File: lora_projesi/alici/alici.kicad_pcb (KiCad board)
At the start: 4 copper layers, 88 x 102 mm, 127 parts, among them J1 USB-C, J2 SMA, J3 RJ45, J4 u.FL (ANA ANTEN), J5 12 V GIRIS, J6 LAMBA, J7 MICRO-SIM, J8 u.FL (YARDIMCI ANTEN, ISTEGE 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, K1 SRD-12VDC-SL-A, Q1 AO3401A, Q2 MMBT2222A, Q3 MMBT2222A, Q4 MMBT2222A, SW1 DUGME, U1 ESP32-S3-WROOM-1-N4, U10 SIM7600SA, U11 AP2112K-3.3, U12 ESDA6V1-5SC6, U4 RFM95W-915S2, U5 TPS62933DRLR, U6 TPS62933DRLR, U7 USBLC6-2SC6, U8 TXB0104PW, U9 W5500, Y1 25 MHz

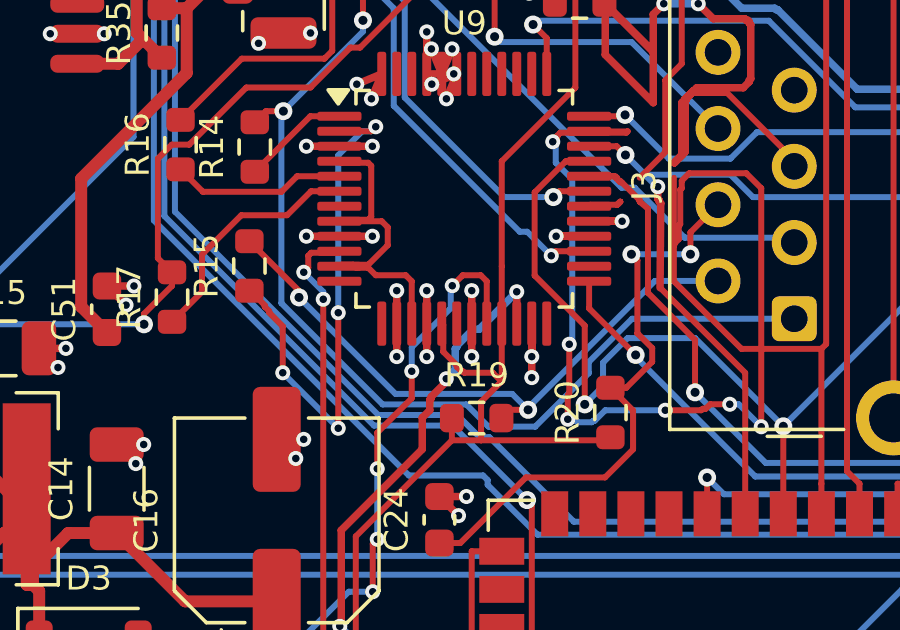
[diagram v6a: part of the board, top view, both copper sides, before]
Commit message: Alici: pin 16 dis toprak via kaldirildi, yonlendirme suruyor
Co-Authored-By: Claude Sonnet 5.5 <noreply@anthropic.com>
Claude-Session: https://claude.ai/code/session_01Q71gHQtKJ86ZE2CtYTYSwP
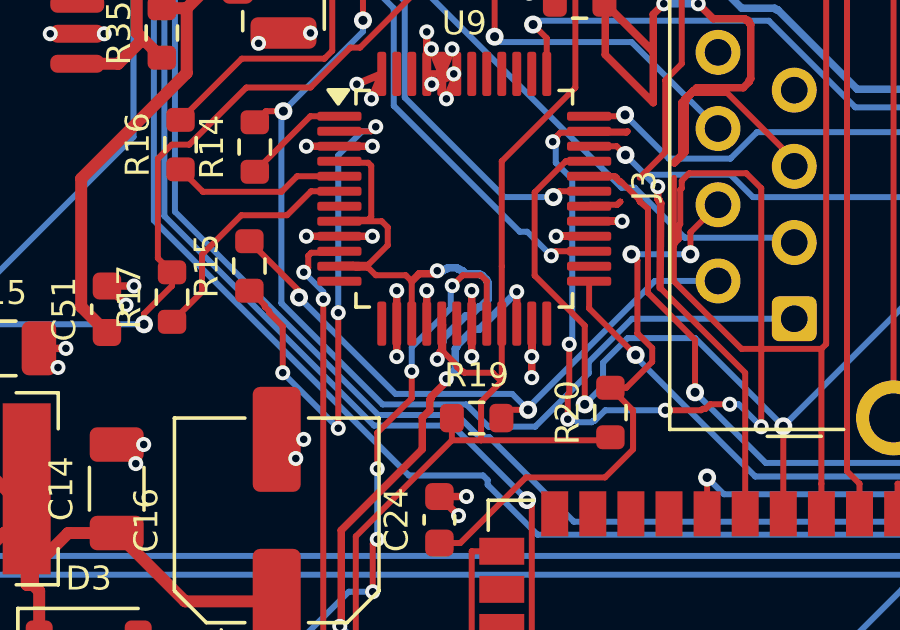
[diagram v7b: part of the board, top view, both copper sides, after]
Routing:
- net +3V3A: track 80.8 -> 88.5 mm, vias 0 -> 2
- net GND: track 230.0 -> 228.9 mm, vias 234 -> 233
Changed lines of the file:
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@@
   (segment (start 55.5882 70.0518) (end 55.5882 69.3114) (width 0.2) (layer "F.Cu") (net 4))
   (segment (start 55.75 67.55) (end 55.75 67.6) (width 0.2) (layer "F.Cu") (net 4))
+  (segment (start 55.2 67.1) (end 55.25 67.05) (width 0.25) (layer "F.Cu") (net 4))
   (segment (start 55.25 66.15) (end 55.3 66.2) (width 0.2) (layer "F.Cu") (net 4))
   (segment (start 60.7702 70.0518) (end 60.8715 69.9505) (width 0.2) (layer "F.Cu") (net 4))
@@
   (segment (start 58.7075 52.4276) (end 58.7075 52.1556) (width 0.2) (layer "F.Cu") (net 4))
   (segment (start 55.5496 48.9977) (end 54.9573 48.9977) (width 0.2) (layer "F.Cu") (net 4))
+  (segment (start 55 64.5) (end 55.1 64.4) (width 0.25) (layer "F.Cu") (net 4))
   (segment (start 55.9 67.75) (end 55.95 67.75) (width 0.2) (layer "F.Cu") (net 4))
+  (segment (start 54.5 64.5) (end 55 64.5) (width 0.25) (layer "F.Cu") (net 4))
   (segment (start 57.25 68.0782) (end 57.25 66.1625) (width 0.2) (layer "F.Cu") (net 4))
   (segment (start 52.8 64.2) (end 53.45 63.55) (width 0.2) (layer "F.Cu") (net 4))
   (segment (start 54.4061 52.6335) (end 54.4061 53.9598) (width 0.2) (layer "F.Cu") (net 4))
   (segment (start 57.25 60.75) (end 57.25 64.25) (width 0.2) (layer "F.Cu") (net 4))
+  (segment (start 55.1 67.35) (end 55.2 67.25) (width 0.25) (layer "F.Cu") (net 4))
   (segment (start 53.45 62.95) (end 53.25 62.75) (width 0.2) (layer "F.Cu") (net 4))
   (segment (start 54.222 48.9977) (end 53.6613 48.437) (width 0.2) (layer "F.Cu") (net 4))
@@
   (segment (start 52.3845 73.2555) (end 52.3845 79.1916) (width 0.2) (layer "F.Cu") (net 4))
   (segment (start 54.05 64.55) (end 54.25 64.75) (width 0.2) (layer "F.Cu") (net 4))
+  (segment (start 54.25 64.75) (end 54.5 64.5) (width 0.25) (layer "F.Cu") (net 4))
   (segment (start 56.5607 70.0518) (end 55.5882 70.0518) (width 0.2) (layer "F.Cu") (net 4))
   (segment (start 55.3 66.2) (end 55.3 67.1) (width 0.2) (layer "F.Cu") (net 4))
   (segment (start 51.9 64.2) (end 52.8 64.2) (width 0.2) (layer "F.Cu") (net 4))
+  (segment (start 55.2 67.25) (end 55.2 67.1) (width 0.25) (layer "F.Cu") (net 4))
   (segment (start 56.5607 70.0518) (end 60.7702 70.0518) (width 0.2) (layer "F.Cu") (net 4))
   (segment (start 61.6665 50.1847) (end 59.7039 52.1473) (width 0.2) (layer "F.Cu") (net 4))
@@
   (segment (start 56.5607 70.0518) (end 56.5607 68.7675) (width 0.2) (layer "F.Cu") (net 4))
   (segment (start 51.9 62.7) (end 52.8 62.7) (width 0.2) (layer "F.Cu") (net 4))
+  (segment (start 55.25 67.05) (end 55.25 66.15) (width 0.25) (layer "F.Cu") (net 4))
   (segment (start 52.6349 81.6536) (end 52.3845 81.4032) (width 0.2) (layer "F.Cu") (net 4))
   (segment (start 54.222 52.4494) (end 54.4061 52.6335) (width 0.2) (layer "F.Cu") (net 4))
@@
   (segment (start 52.3845 81.4032) (end 52.3845 79.1916) (width 0.2) (layer "F.Cu") (net 4))
   (segment (start 56.5607 68.7675) (end 57.25 68.0782) (width 0.2) (layer "F.Cu") (net 4))
+  (via (at 55.1 67.35) (size 0.5) (drill 0.25) (layers "F.Cu" "B.Cu") (net 4))
+  (via (at 55.1 64.4) (size 0.5) (drill 0.25) (layers "F.Cu" "B.Cu") (net 4))
+  (segment (start 56.65 65.5) (end 56.65 65.55) (width 0.25) (layer "B.Cu") (net 4))
+  (segment (start 55.3 64.4) (end 55.35 64.35) (width 0.25) (layer "B.Cu") (net 4))
+  (segment (start 56.6 65.55) (end 56.55 65.6) (width 0.25) (layer "B.Cu") (net 4))
+  (segment (start 55.75 64.3) (end 55.8 64.35) (width 0.25) (layer "B.Cu") (net 4))
+  (segment (start 56.7 65.5) (end 56.65 65.5) (width 0.25) (layer "B.Cu") (net 4))
+  (segment (start 55.1 64.4) (end 55.3 64.4) (width 0.25) (layer "B.Cu") (net 4))
+  (segment (start 56.75 65.4) (end 56.75 65.45) (width 0.25) (layer "B.Cu") (net 4))
+  (segment (start 55.8 64.35) (end 55.85 64.35) (width 0.25) (layer "B.Cu") (net 4))
+  (segment (start 55.45 64.3) (end 55.75 64.3) (width 0.25) (layer "B.Cu") (net 4))
+  (segment (start 56.55 64.55) (end 56.6 64.55) (width 0.25) (layer "B.Cu") (net 4))
+  (segment (start 55.25 67.2) (end 55.1 67.35) (width 0.25) (layer "B.Cu") (net 4))
+  (segment (start 55.4 64.35) (end 55.45 64.3) (width 0.25) (layer "B.Cu") (net 4))
+  (segment (start 55.95 64.4) (end 56.05 64.5) (width 0.25) (layer "B.Cu") (net 4))
+  (segment (start 56.5 64.5) (end 56.55 64.55) (width 0.25) (layer "B.Cu") (net 4))
+  (segment (start 55.9 64.4) (end 55.95 64.4) (width 0.25) (layer "B.Cu") (net 4))
+  (segment (start 55.25 66.8) (end 55.25 67.2) (width 0.25) (layer "B.Cu") (net 4))
+  (segment (start 56.05 64.5) (end 56.5 64.5) (width 0.25) (layer "B.Cu") (net 4))
+  (segment (start 55.3 66.75) (end 55.25 66.8) (width 0.25) (layer "B.Cu") (net 4))
+  (segment (start 56.6 64.55) (end 56.75 64.7) (width 0.25) (layer "B.Cu") (net 4))
+  (segment (start 55.3 66.65) (end 55.3 66.75) (width 0.25) (layer "B.Cu") (net 4))
+  (segment (start 56.5 65.6) (end 56.2 65.9) (width 0.25) (layer "B.Cu") (net 4))
+  (segment (start 56.75 65.45) (end 56.7 65.45) (width 0.25) (layer "B.Cu") (net 4))
+  (segment (start 56.05 65.9) (end 55.3 66.65) (width 0.25) (layer "B.Cu") (net 4))
+  (segment (start 56.55 65.6) (end 56.5 65.6) (width 0.25) (layer "B.Cu") (net 4))
+  (segment (start 56.75 64.75) (end 56.8 64.8) (width 0.25) (layer "B.Cu") (net 4))
+  (segment (start 56.65 65.55) (end 56.6 65.55) (width 0.25) (layer "B.Cu") (net 4))
+  (segment (start 55.85 64.35) (end 55.9 64.4) (width 0.25) (layer "B.Cu") (net 4))
+  (segment (start 56.75 64.7) (end 56.75 64.75) (width 0.25) (layer "B.Cu") (net 4))
+  (segment (start 56.8 65.35) (end 56.75 65.4) (width 0.25) (layer "B.Cu") (net 4))
+  (segment (start 55.35 64.35) (end 55.4 64.35) (width 0.25) (layer "B.Cu") (net 4))
+  (segment (start 56.8 64.8) (end 56.8 65.35) (width 0.25) (layer "B.Cu") (net 4))
+  (segment (start 56.7 65.45) (end 56.7 65.5) (width 0.25) (layer "B.Cu") (net 4))
+  (segment (start 56.2 65.9) (end 56.05 65.9) (width 0.25) (layer "B.Cu") (net 4))
   (segment (start 3.4987 93.8653) (end 4.1572 93.8653) (width 0.2) (layer "F.Cu") (net 5))
   (segment (start 4.1572 93.8653) (end 5.6611 92.3614) (width 0.2) (layer "F.Cu") (net 5))
@@
   (segment (start 12.9 45.5) (end 13.8 45.5) (width 0.25) (layer "F.Cu") (net 93))
   (segment (start 30.250064 68.42492) (end 31.150063 68.42492) (width 0.25) (layer "F.Cu") (net 93))
-  (segment (start 54.75 66.1625) (end 54.75 67.262499) (width 0.25) (layer "F.Cu") (net 93))
   (segment (start 7.773115 46.305686) (end 8.673115 46.305686) (width 0.25) (layer "F.Cu") (net 93))
   (segment (start 34.5 31.9) (end 34.5 31) (width 0.25) (layer "F.Cu") (net 93))
@@
   (via (at 57.613603 5.136396) (size 0.5) (drill 0.25) (layers "F.Cu" "B.Cu") (net 93))
   (via (at 65.83836 40.358364) (size 0.5) (drill 0.25) (layers "F.Cu" "B.Cu") (net 93))
-  (via (at 54.75 67.262499) (size 0.5) (drill 0.25) (layers "F.Cu" "B.Cu") (net 93))
   (via (at 78.425 23) (size 0.5) (drill 0.25) (layers "F.Cu" "B.Cu") (net 93))
   (via (at 51.818797 12.056545) (size 0.5) (drill 0.25) (layers "F.Cu" "B.Cu") (net 93))

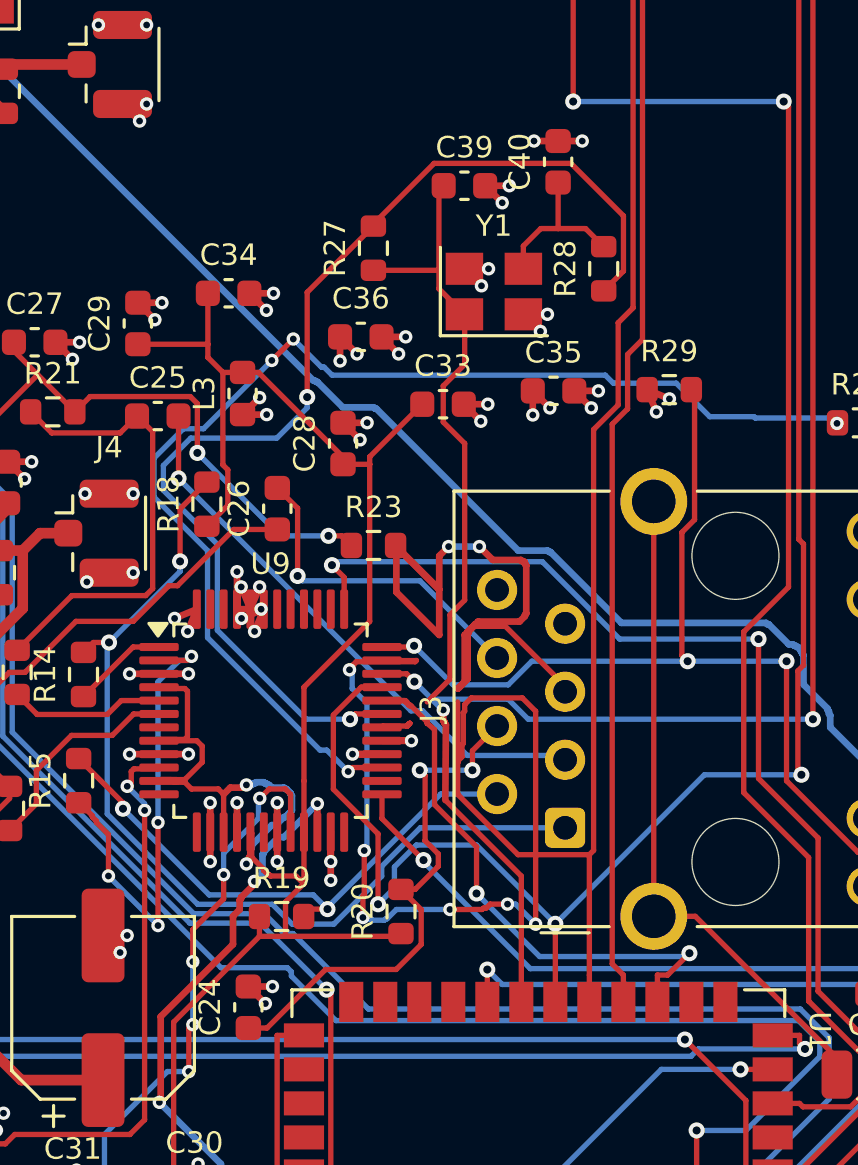
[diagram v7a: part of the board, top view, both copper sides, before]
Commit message: Alici: +3V3A cozuldu, XI/XO/ETH_CS oncelikli yeniden cizim
Co-Authored-By: Claude Sonnet 5.5 <noreply@anthropic.com>
Claude-Session: https://claude.ai/code/session_01Q71gHQtKJ86ZE2CtYTYSwP
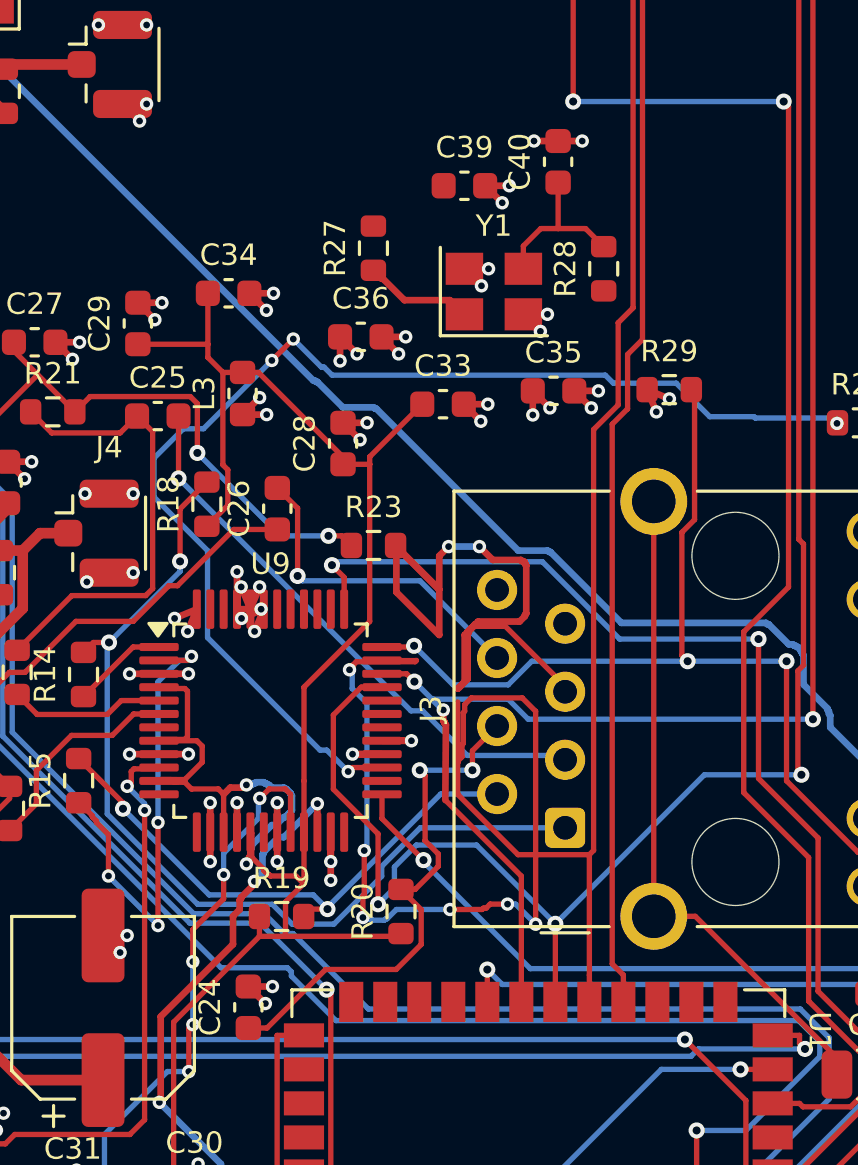
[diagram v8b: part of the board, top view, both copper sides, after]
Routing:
- net XO: track 42.9 -> 0.00 mm, vias 2 -> 0
- net ETH_CS: track 21.8 -> 0.00 mm, vias 2 -> 0
- net XI: track 25.1 -> 4.08 mm
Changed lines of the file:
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@@
   (segment (start 76.3781 89.9365) (end 76.3781 87.7731) (width 0.2) (layer "F.Cu") (net 19))
   (segment (start 76.325 87.72) (end 77.15 86.895) (width 0.2) (layer "F.Cu") (net 19))
-  (segment (start 61.25 61.45) (end 61.85 62.05) (width 0.2) (layer "F.Cu") (net 20))
-  (segment (start 61.15 61.4) (end 61.05 61.3) (width 0.2) (layer "F.Cu") (net 20))
-  (segment (start 61 61.25) (end 61.05 61.3) (width 0.2) (layer "F.Cu") (net 20))
-  (segment (start 63.6935 66.7046) (end 63.6935 68.4525) (width 0.2) (layer "F.Cu") (net 20))
-  (segment (start 70.8259 71.4983) (end 71.6417 70.6825) (width 0.2) (layer "F.Cu") (net 20))
-  (segment (start 61.85 62.05) (end 61.85 62.1) (width 0.2) (layer "F.Cu") (net 20))
-  (segment (start 62.1241 62.3294) (end 61.85 62.1) (width 0.2) (layer "F.Cu") (net 20))
-  (segment (start 60.15 61.25) (end 61 61.25) (width 0.2) (layer "F.Cu") (net 20))
-  (segment (start 70.445 71.4983) (end 70.8259 71.4983) (width 0.2) (layer "F.Cu") (net 20))
-  (segment (start 61.2 61.45) (end 61.15 61.4) (width 0.2) (layer "F.Cu") (net 20))
-  (segment (start 61.85 62.1) (end 61.85 62.05) (width 0.2) (layer "F.Cu") (net 20))
-  (segment (start 70.445 72.5) (end 70.445 71.4983) (width 0.2) (layer "F.Cu") (net 20))
-  (segment (start 60.1625 61.25) (end 61.0447 61.25) (width 0.2) (layer "F.Cu") (net 20))
-  (segment (start 61.15 61.4) (end 61.2 61.4) (width 0.2) (layer "F.Cu") (net 20))
-  (segment (start 61.25 61.45) (end 61.2 61.45) (width 0.2) (layer "F.Cu") (net 20))
-  (segment (start 62.1241 62.3294) (end 62.1241 65.1352) (width 0.2) (layer "F.Cu") (net 20))
-  (segment (start 61.05 61.3) (end 61.1 61.3) (width 0.2) (layer "F.Cu") (net 20))
-  (segment (start 62.1241 65.1352) (end 63.6935 66.7046) (width 0.2) (layer "F.Cu") (net 20))
-  (via (at 63.6935 68.4525) (size 0.6) (drill 0.3) (layers "F.Cu" "B.Cu") (net 20))
-  (via (at 71.6417 70.6825) (size 0.6) (drill 0.3) (layers "F.Cu" "B.Cu") (net 20))
-  (segment (start 71.5175 70.8067) (end 66.0477 70.8067) (width 0.2) (layer "B.Cu") (net 20))
-  (segment (start 71.6417 70.6825) (end 71.5175 70.8067) (width 0.2) (layer "B.Cu") (net 20))
-  (segment (start 66.0477 70.8067) (end 63.6935 68.4525) (width 0.2) (layer "B.Cu") (net 20))
   (segment (start 75.2676 59.7806) (end 75.2676 64.2455) (width 0.2) (layer "F.Cu") (net 21))
   (segment (start 79.2988 68.5629) (end 78.9301 68.9316) (width 0.2) (layer "F.Cu") (net 21))
@@
   (segment (start 66.0895 43.6271) (end 66.7384 43.6271) (width 0.2) (layer "F.Cu") (net 90))
   (segment (start 67.7648 43.6271) (end 68.4405 44.3028) (width 0.2) (layer "F.Cu") (net 90))
-  (segment (start 60.15 62.25) (end 60.2 62.2) (width 0.2) (layer "F.Cu") (net 91))
-  (segment (start 63.2405 46.8278) (end 62.2888 45.8761) (width 0.2) (layer "F.Cu") (net 91))
-  (segment (start 61.1 62.2) (end 61.2 62.1) (width 0.2) (layer "F.Cu") (net 91))
-  (segment (start 62.2888 42.2045) (end 62.4655 42.0278) (width 0.2) (layer "F.Cu") (net 91))
-  (segment (start 61.1 62.2) (end 61.2 62.1) (width 0.2) (layer "F.Cu") (net 91))
-  (segment (start 63.25 48.7) (end 63.25 46.85) (width 0.2) (layer "F.Cu") (net 91))
-  (segment (start 62.2888 45.1841) (end 62.2888 42.2045) (width 0.2) (layer "F.Cu") (net 91))
-  (segment (start 60.2 62.2) (end 61.1 62.2) (width 0.2) (layer "F.Cu") (net 91))
-  (segment (start 61.1 62.2) (end 61.2 62.1) (width 0.2) (layer "F.Cu") (net 91))
-  (segment (start 61.85 61.3) (end 62.7 60.45) (width 0.2) (layer "F.Cu") (net 91))
-  (segment (start 62.2888 45.1841) (end 59.8426 45.1841) (width 0.2) (layer "F.Cu") (net 91))
-  (segment (start 62.7 60.45) (end 62.7 58.05) (width 0.2) (layer "F.Cu") (net 91))
-  (segment (start 61.1 62.2) (end 61.2 62.1) (width 0.2) (layer "F.Cu") (net 91))
-  (segment (start 62.45 50.85) (end 62.45 49.5) (width 0.2) (layer "F.Cu") (net 91))
-  (segment (start 62.45 49.5) (end 63.25 48.7) (width 0.2) (layer "F.Cu") (net 91))
-  (segment (start 63.25 51.65) (end 62.45 50.85) (width 0.2) (layer "F.Cu") (net 91))
-  (segment (start 62.2888 45.8761) (end 62.2888 45.1841) (width 0.2) (layer "F.Cu") (net 91))
-  (segment (start 62.7 58.05) (end 63.25 57.5) (width 0.2) (layer "F.Cu") (net 91))
-  (segment (start 63.25 57.5) (end 63.25 51.65) (width 0.2) (layer "F.Cu") (net 91))
-  (segment (start 61.1 62.2) (end 61.2 62.1) (width 0.2) (layer "F.Cu") (net 91))
-  (segment (start 57.3696 49.9189) (end 57.3696 46.0071) (width 0.2) (layer "F.Cu") (net 92))
-  (segment (start 59.8426 43.4584) (end 62.1083 41.1927) (width 0.2) (layer "F.Cu") (net 92))
-  (segment (start 69.178 45.2153) (end 68.4405 45.9528) (width 0.2) (layer "F.Cu") (net 92))
-  (segment (start 69.178 43.1518) (end 69.178 45.2153) (width 0.2) (layer "F.Cu") (net 92))
-  (segment (start 67.2189 41.1927) (end 69.178 43.1518) (width 0.2) (layer "F.Cu") (net 92))
-  (segment (start 62.1083 41.1927) (end 67.2189 41.1927) (width 0.2) (layer "F.Cu") (net 92))
-  (segment (start 59.1646 61.75) (end 58.9706 61.944) (width 0.2) (layer "F.Cu") (net 92))
-  (segment (start 60.1625 61.75) (end 59.1646 61.75) (width 0.2) (layer "F.Cu") (net 92))
-  (segment (start 59.8426 43.5341) (end 59.8426 43.4584) (width 0.2) (layer "F.Cu") (net 92))
-  (segment (start 57.3696 46.0071) (end 59.8426 43.5341) (width 0.2) (layer "F.Cu") (net 92))
-  (via (at 58.9706 61.944) (size 0.6) (drill 0.3) (layers "F.Cu" "B.Cu") (net 92))
-  (via (at 57.3696 49.9189) (size 0.6) (drill 0.3) (layers "F.Cu" "B.Cu") (net 92))
-  (segment (start 57.3341 61.944) (end 58.9706 61.944) (width 0.2) (layer "B.Cu") (net 92))
-  (segment (start 52.0004 52.4722) (end 52.0004 53.4006) (width 0.2) (layer "B.Cu") (net 92))
-  (segment (start 53.0212 51.4514) (end 52.0004 52.4722) (width 0.2) (layer "B.Cu") (net 92))
-  (segment (start 54.016 58.6259) (end 57.3341 61.944) (width 0.2) (layer "B.Cu") (net 92))
-  (segment (start 57.3696 49.9189) (end 57.3695 49.9189) (width 0.2) (layer "B.Cu") (net 92))
-  (segment (start 54.016 55.4162) (end 54.016 58.6259) (width 0.2) (layer "B.Cu") (net 92))
-  (segment (start 56.2346 51.4514) (end 53.0212 51.4514) (width 0.2) (layer "B.Cu") (net 92))
-  (segment (start 52.0004 53.4006) (end 54.016 55.4162) (width 0.2) (layer "B.Cu") (net 92))
-  (segment (start 57.3695 49.9189) (end 57.3695 50.3165) (width 0.2) (layer "B.Cu") (net 92))
-  (segment (start 57.3695 50.3165) (end 56.2346 51.4514) (width 0.2) (layer "B.Cu") (net 92))
+  (segment (start 62.7 46.3) (end 63.2405 46.8278) (width 0.25) (layer "F.Cu") (net 91))
+  (segment (start 60.15 45.5) (end 60.2 45.5) (width 0.25) (layer "F.Cu") (net 91))
+  (segment (start 59.8426 45.1841) (end 60.15 45.5) (width 0.25) (layer "F.Cu") (net 91))
+  (segment (start 60.2 45.5) (end 61 46.3) (width 0.25) (layer "F.Cu") (net 91))
+  (segment (start 61 46.3) (end 62.7 46.3) (width 0.25) (layer "F.Cu") (net 91))
   (segment (start 31.097674 72.81632) (end 31.73407 73.452716) (width 0.25) (layer "F.Cu") (net 93))
   (segment (start 77.525 9) (end 78.161396 9.636396) (width 0.25) (layer "F.Cu") (net 93))
